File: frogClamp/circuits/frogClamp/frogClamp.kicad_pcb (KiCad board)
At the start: 2 copper layers, 4 x 13.5 mm, 5 parts

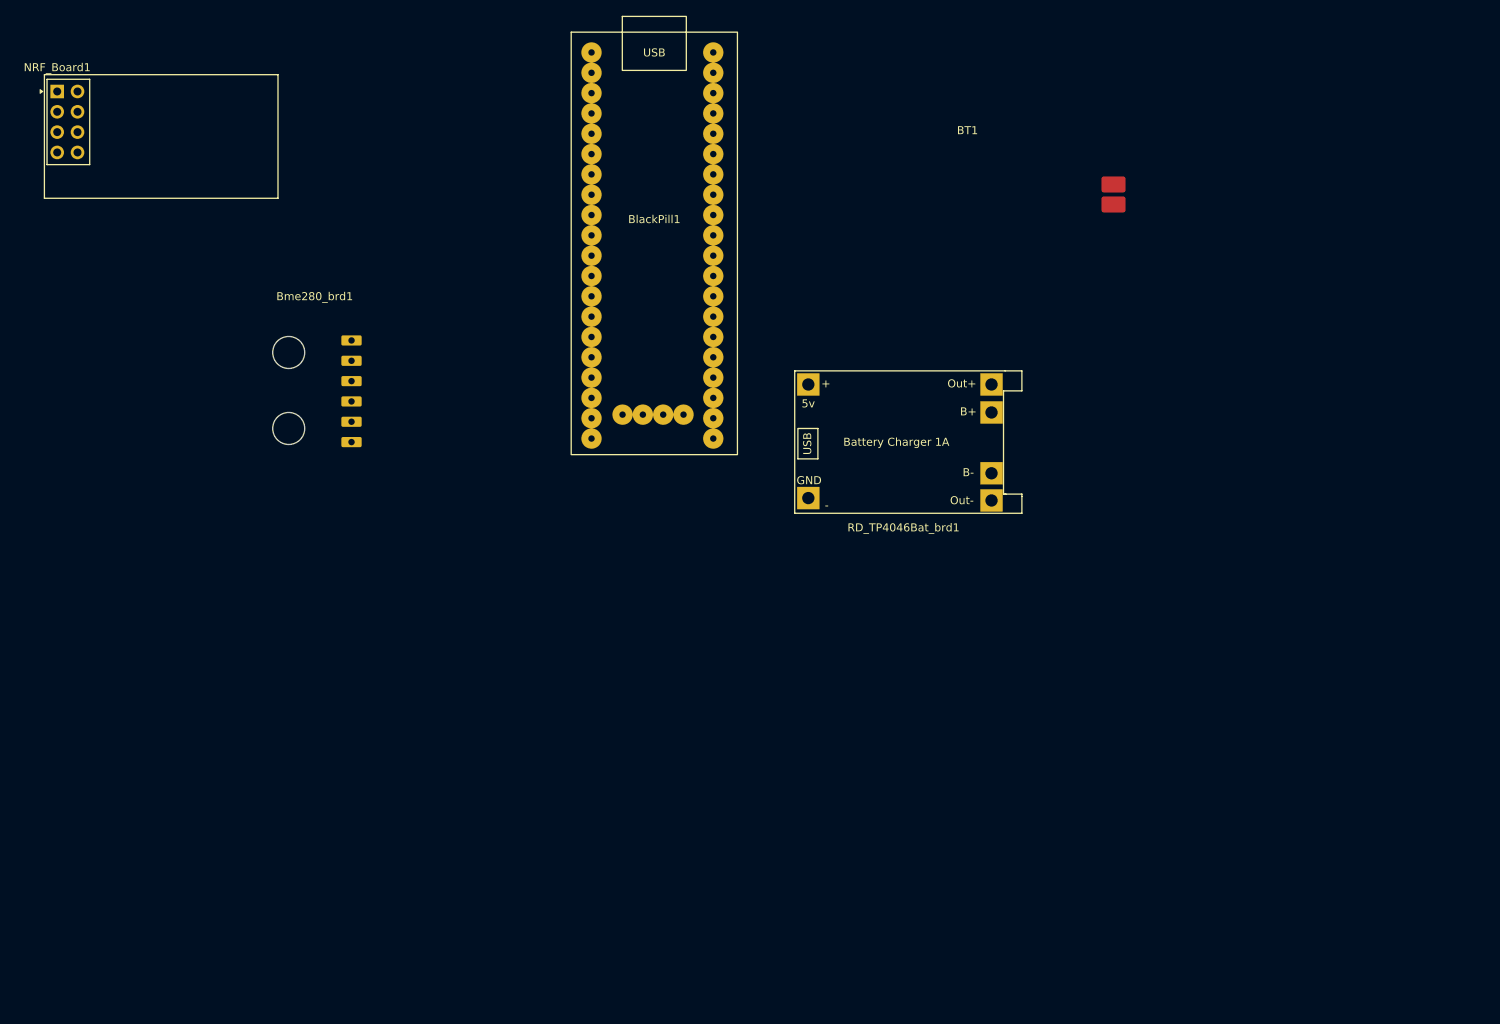
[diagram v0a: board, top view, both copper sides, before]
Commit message: Added libraries to project
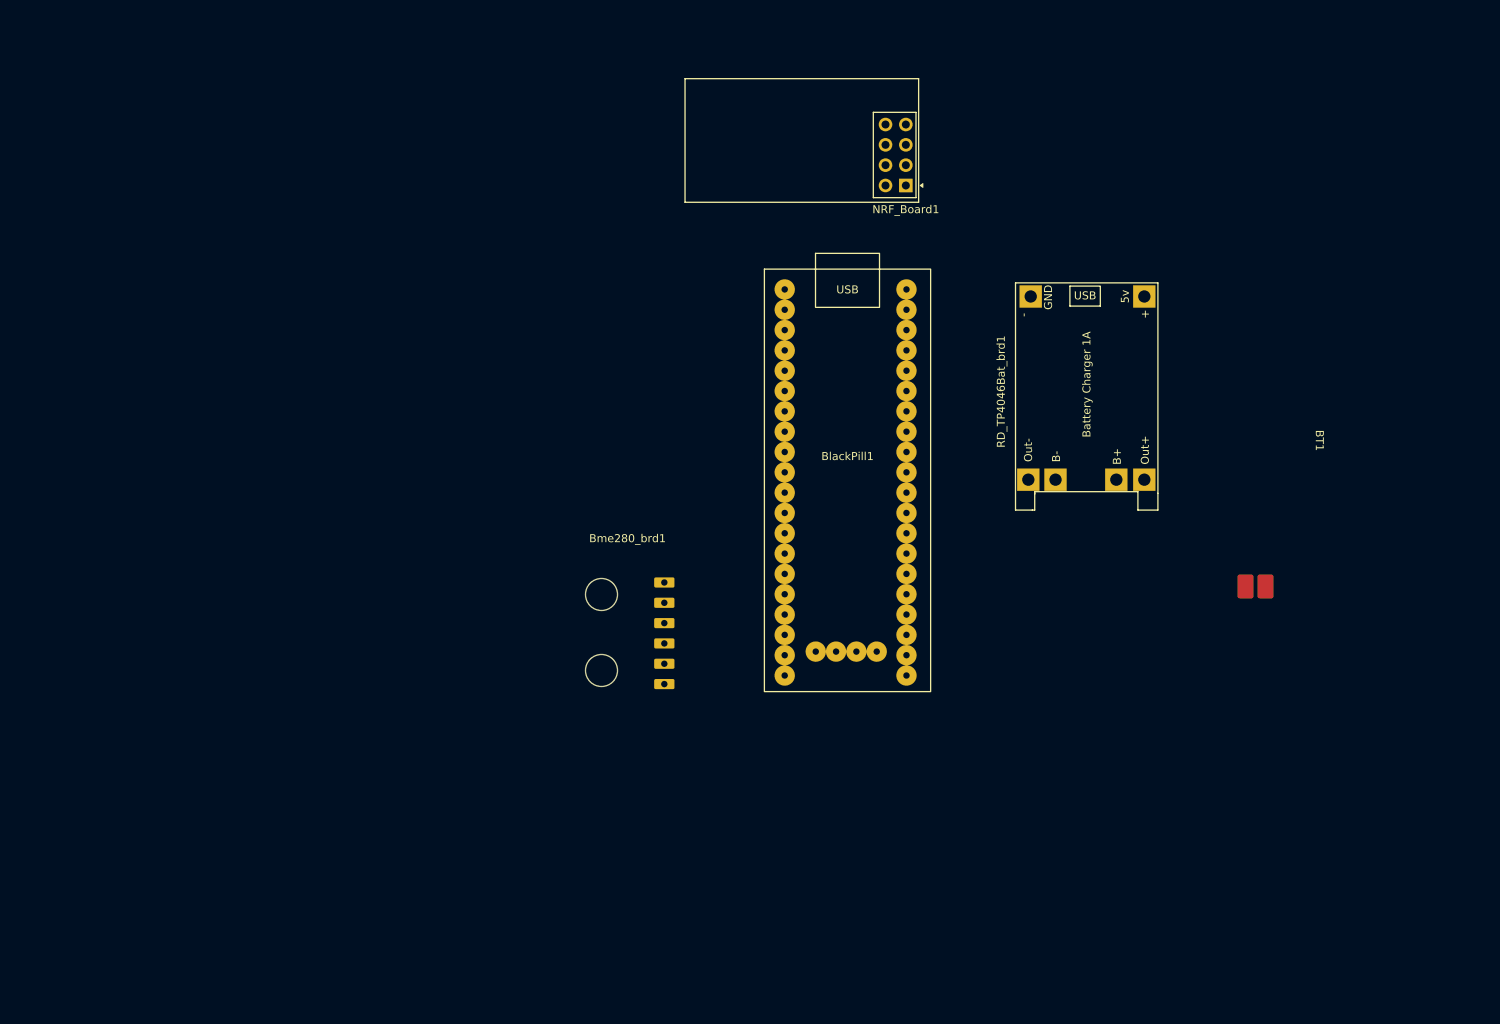
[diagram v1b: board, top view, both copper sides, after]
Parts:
- moved NRF_Board1 106.7 mm to (177.8, 48.6), turned to 180 degrees
- moved BT1 57.2 mm to (228.5, 80.5), turned to -90 degrees
- moved Bme280_brd1 49.4 mm to (143.0, 104.5)
- moved BlackPill1 38.2 mm to (170.5, 85.5)
- moved RD_TP4046Bat_brd1 36.2 mm to (200.0, 74.5), turned to -90 degrees
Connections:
- BT1 pad 1: unconnected-(BT1-+-Pad1) -> Net-(BT1-+)
- BT1 pad 2: unconnected-(BT1---Pad2) -> Net-(BT1--)
- BlackPill1 pad 14: unconnected-(BlackPill1-PB6-Pad14) -> SCL
- BlackPill1 pad 15: unconnected-(BlackPill1-PB7-Pad15) -> SDA
- BlackPill1 pad 19: unconnected-(BlackPill1-GND-Pad19) -> Net-(Bme280_brd1-GND)
- BlackPill1 pad 20: unconnected-(BlackPill1-3.3V-Pad20) -> Net-(Bme280_brd1-VIN)
- BlackPill1 pad 21: unconnected-(BlackPill1-5V-Pad21) -> Net-(RD_TP4046Bat_brd1-Out+)
- BlackPill1 pad 22: unconnected-(BlackPill1-GND-Pad22) -> Net-(NRF_Board1-GND)
- BlackPill1 pad 23: unconnected-(BlackPill1-3.3V-Pad23) -> Net-(NRF_Board1-VCC)
- Bme280_brd1 pad 1: unconnected-(Bme280_brd1-VIN-Pad1) -> Net-(Bme280_brd1-VIN)
- Bme280_brd1 pad 2: unconnected-(Bme280_brd1-GND-Pad2) -> Net-(Bme280_brd1-GND)
- Bme280_brd1 pad 3: unconnected-(Bme280_brd1-SCL-Pad3) -> SCL
- Bme280_brd1 pad 4: unconnected-(Bme280_brd1-SDA-Pad4) -> SDA
- NRF_Board1 pad 1: unconnected-(NRF_Board1-GND-Pad1) -> Net-(NRF_Board1-GND)
- NRF_Board1 pad 2: unconnected-(NRF_Board1-VCC-Pad2) -> Net-(NRF_Board1-VCC)
- RD_TP4046Bat_brd1 pad 3: unconnected-(RD_TP4046Bat_brd1-Out+-Pad3) -> Net-(RD_TP4046Bat_brd1-Out+)
- RD_TP4046Bat_brd1 pad 4: unconnected-(RD_TP4046Bat_brd1-B+-Pad4) -> Net-(BT1-+)
- RD_TP4046Bat_brd1 pad 5: unconnected-(RD_TP4046Bat_brd1-B--Pad5) -> Net-(BT1--)
- RD_TP4046Bat_brd1 pad 6: unconnected-(RD_TP4046Bat_brd1-Out--Pad6) -> Net-(NRF_Board1-GND)

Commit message: finished schematic, rough board layout
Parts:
- added BZ1: Buzzer, Crystal:Resonator-2Pin_W6.0mm_H3.0mm, F.Cu at (182.0, 81.1)
- added D1: 1N5407, Diode_SMD:D_1206_3216Metric_Pad1.42x1.75mm_HandSolder, F.Cu at (202.0, 69.5)
- added D2: 1N5407, Diode_SMD:D_1206_3216Metric_Pad1.42x1.75mm_HandSolder, F.Cu at (202.0, 61.0)
- added M1: Motor Pump, AARobin:miniPump_1.2, F.Cu at (244.5, 94.5)
- added M2: Solenoid Valve, AARobin:SolenoidValve_9.0, F.Cu at (215.0, 55.5)
- added Q1: QM6006D, Package_TO_SOT_SMD:TO-252-2, F.Cu at (194.0, 70.3)
- added Q2: QM6006D, Package_TO_SOT_SMD:TO-252-2, F.Cu at (194.0, 61.1)
- added R1: 10k, Resistor_SMD:R_1206_3216Metric, F.Cu at (184.0, 72.8)
- added R2: 100, Resistor_SMD:R_1206_3216Metric, F.Cu at (184.0, 67.8)
- added R3: 100, Resistor_SMD:R_1206_3216Metric, F.Cu at (184.0, 58.6)
- added R4: 10k, Resistor_SMD:R_1206_3216Metric, F.Cu at (184.0, 63.6)
- added SW1: SW_SPDT, Button_Switch_SMD:SW_SPST_B3U-1100P, F.Cu at (152.5, 51.5)
- BT1: moved to B.Cu
- NRF_Board1: footprint RF_Module:nRF24L01_Breakout -> AARobin:nRF24L01_Breakout
- moved BT1 115.5 mm to (113.0, 76.0)
- moved RD_TP4046Bat_brd1 96.4 mm to (111.8, 113.5), turned to 0 degrees
- moved Bme280_brd1 71.7 mm to (214.6, 102.5), turned to -90 degrees
- moved NRF_Board1 51.8 mm to (135.4, 78.3), turned to 90 degrees
- moved BlackPill1 7.50 mm to (168.1, 78.4)
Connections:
- net Net-(BT1--) renamed B-
- BT1 pad 1: Net-(BT1-+) -> B+
- BlackPill1 pad 1: unconnected-(BlackPill1-PB12-Pad1) -> NRF_CE
- BlackPill1 pad 19: Net-(Bme280_brd1-GND) -> GND
- BlackPill1 pad 2: unconnected-(BlackPill1-PB13-Pad2) -> NRF_SCK
- BlackPill1 pad 20: Net-(Bme280_brd1-VIN) -> 3.3V
- BlackPill1 pad 21: Net-(RD_TP4046Bat_brd1-Out+) -> Net-(SW1-A)
- BlackPill1 pad 22: Net-(NRF_Board1-GND) -> GND
- BlackPill1 pad 23: Net-(NRF_Board1-VCC) -> 3.3V
- BlackPill1 pad 24: unconnected-(BlackPill1-PB10-Pad24) -> NRF_SCK
- BlackPill1 pad 26: unconnected-(BlackPill1-PB1-Pad26) -> VALVE
- BlackPill1 pad 27: unconnected-(BlackPill1-PB0-Pad27) -> PUMP
- BlackPill1 pad 28: unconnected-(BlackPill1-PA7-Pad28) -> SPKR
- BlackPill1 pad 29: unconnected-(BlackPill1-PA6-Pad29) -> PWR_LED
- BlackPill1 pad 3: unconnected-(BlackPill1-PB14-Pad3) -> NRF_MOSI
- BlackPill1 pad 4: unconnected-(BlackPill1-PB15-Pad4) -> NRF_MISO
- BlackPill1 pad 40: unconnected-(BlackPill1-VB-Pad40) -> B+
- Bme280_brd1 pad 1: Net-(Bme280_brd1-VIN) -> 3.3V
- Bme280_brd1 pad 2: Net-(Bme280_brd1-GND) -> GND
- NRF_Board1 pad 1: Net-(NRF_Board1-GND) -> GND
- NRF_Board1 pad 2: Net-(NRF_Board1-VCC) -> 3.3V
- NRF_Board1 pad 3: unconnected-(NRF_Board1-CE-Pad3) -> NRF_CE
- NRF_Board1 pad 4: unconnected-(NRF_Board1-CSN-Pad4) -> NRF_CSN
- NRF_Board1 pad 5: unconnected-(NRF_Board1-SCK-Pad5) -> NRF_SCK
- NRF_Board1 pad 6: unconnected-(NRF_Board1-MOSI-Pad6) -> NRF_MOSI
- NRF_Board1 pad 7: unconnected-(NRF_Board1-MISO-Pad7) -> NRF_MISO
- RD_TP4046Bat_brd1 pad 3: Net-(RD_TP4046Bat_brd1-Out+) -> OUT+
- RD_TP4046Bat_brd1 pad 4: Net-(BT1-+) -> B+
- RD_TP4046Bat_brd1 pad 6: Net-(NRF_Board1-GND) -> GND
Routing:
- net 3.3V: track 0.00 -> 51.5 mm
- net Net-(SW1-A): track 0.00 -> 22.2 mm
- net VALVE: track 0.00 -> 11.6 mm
- net SPKR: track 0.00 -> 11.5 mm
- net Net-(Q2-G): track 0.00 -> 9.84 mm
- net Net-(Q1-G): track 0.00 -> 9.84 mm
- net PUMP: track 0.00 -> 7.87 mm
- net Net-(D2-A): track 0.00 -> 7.35 mm
- net GND: track 0.00 -> 7.21 mm
- net Net-(D1-A): track 0.00 -> 6.99 mm
- net NRF_MISO: track 0.00 -> 1.12 mm
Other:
- board size 4 x 13.5 mm -> 13.5 x 4 mm
